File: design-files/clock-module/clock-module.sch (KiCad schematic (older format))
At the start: 32 parts, among them J101 CUI_PJ-097BH-5_5-2_5mm-5A, Q101 2N6491, SW101 SW_Push, SW102 SW_SPDT, SW103 SW_SPDT, U101 NE555P, U102 NE555P, U103 NE555P, U104 74HCT00, U105 74HCT00

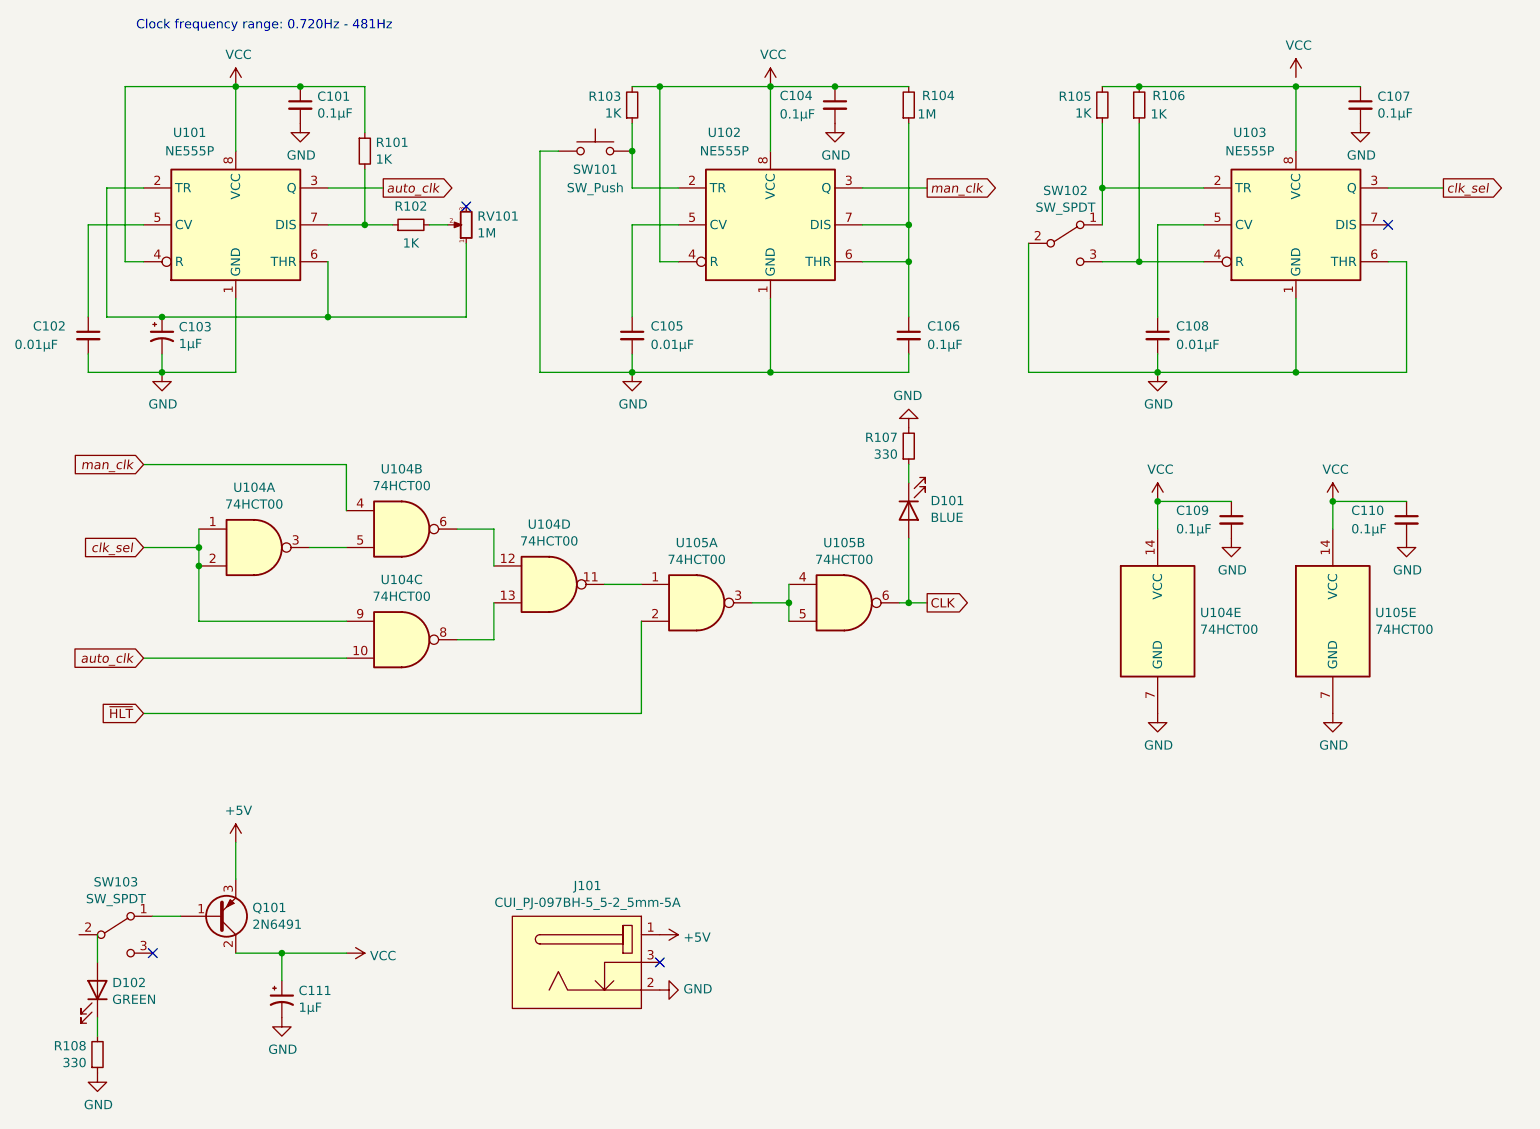
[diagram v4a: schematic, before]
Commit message: clock module: - Don't show the value for each part of a multi-unit device. - Use a green LED for the clock visual.
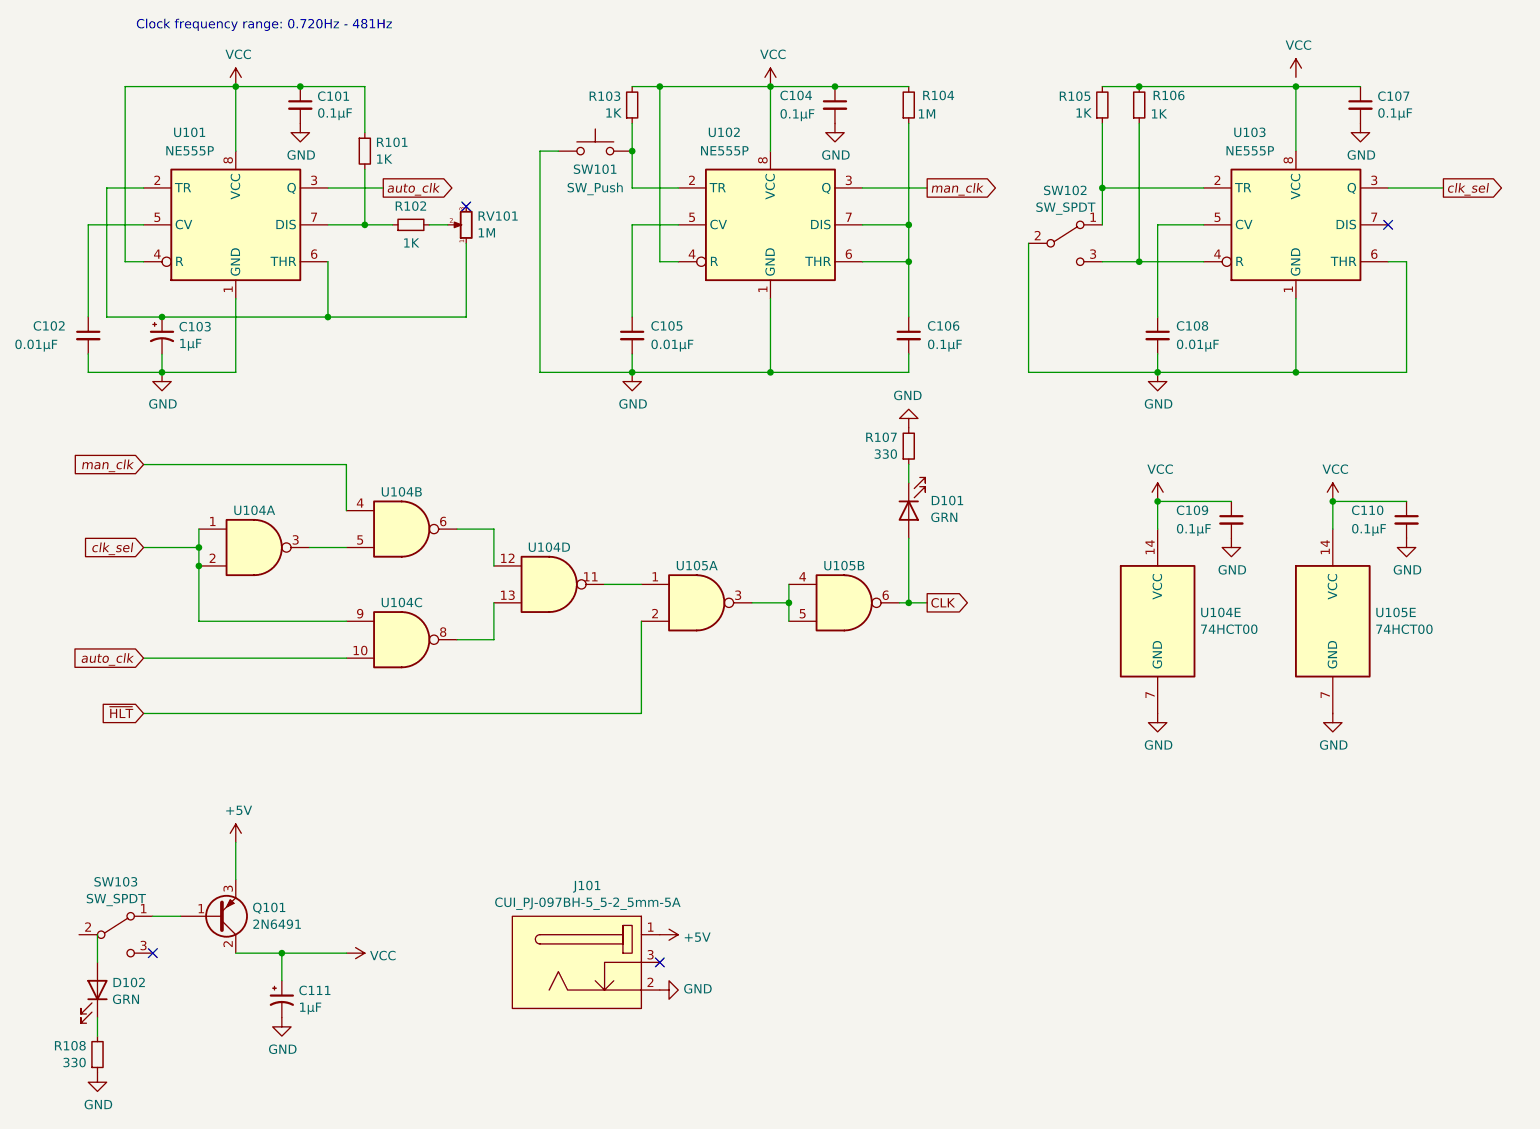
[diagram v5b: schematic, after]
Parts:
- D101: value BLUE -> GRN
- D102: value GREEN -> GRN
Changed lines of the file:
@@
 U 1 1 61BE5527
 P 2250 4050
-F 0 "U104" H 2250 4375 50  0000 C CNN
-F 1 "74HCT00" H 2250 4284 50  0000 C CNN
+F 0 "U104" H 2250 4250 50  0000 C CNN
+F 1 "74HCT00" H 2250 4284 50  0001 C CNN
 F 2 "Package_DIP:DIP-14_W7.62mm_Socket" H 2250 4050 50  0001 C CNN
 F 3 "http://www.ti.com/lit/gpn/sn74hct00" H 2250 4050 50  0001 C CNN
@@
 U 2 1 61BE9444
 P 3050 3950
-F 0 "U104" H 3050 4275 50  0000 C CNN
-F 1 "74HCT00" H 3050 4184 50  0000 C CNN
+F 0 "U104" H 3050 4150 50  0000 C CNN
+F 1 "74HCT00" H 3050 4184 50  0001 C CNN
 F 2 "Package_DIP:DIP-14_W7.62mm_Socket" H 3050 3950 50  0001 C CNN
 F 3 "http://www.ti.com/lit/gpn/sn74hct00" H 3050 3950 50  0001 C CNN
@@
 U 3 1 61BECEBD
 P 3050 4550
-F 0 "U104" H 3050 4875 50  0000 C CNN
-F 1 "74HCT00" H 3050 4784 50  0000 C CNN
+F 0 "U104" H 3050 4750 50  0000 C CNN
+F 1 "74HCT00" H 3050 4784 50  0001 C CNN
 F 2 "Package_DIP:DIP-14_W7.62mm_Socket" H 3050 4550 50  0001 C CNN
 F 3 "http://www.ti.com/lit/gpn/sn74hct00" H 3050 4550 50  0001 C CNN
@@
 U 4 1 61BEEBE7
 P 3850 4250
-F 0 "U104" H 3850 4575 50  0000 C CNN
-F 1 "74HCT00" H 3850 4484 50  0000 C CNN
+F 0 "U104" H 3850 4450 50  0000 C CNN
+F 1 "74HCT00" H 3850 4484 50  0001 C CNN
 F 2 "Package_DIP:DIP-14_W7.62mm_Socket" H 3850 4250 50  0001 C CNN
 F 3 "http://www.ti.com/lit/gpn/sn74hct00" H 3850 4250 50  0001 C CNN
@@
 U 1 1 61C2C1D1
 P 4650 4350
-F 0 "U105" H 4650 4675 50  0000 C CNN
-F 1 "74HCT00" H 4650 4584 50  0000 C CNN
+F 0 "U105" H 4650 4550 50  0000 C CNN
+F 1 "74HCT00" H 4650 4584 50  0001 C CNN
 F 2 "Package_DIP:DIP-14_W7.62mm_Socket" H 4650 4350 50  0001 C CNN
 F 3 "http://www.ti.com/lit/gpn/sn74hct00" H 4650 4350 50  0001 C CNN
@@
 U 2 1 61C30F8B
 P 5450 4350
-F 0 "U105" H 5450 4675 50  0000 C CNN
-F 1 "74HCT00" H 5450 4584 50  0000 C CNN
+F 0 "U105" H 5450 4550 50  0000 C CNN
+F 1 "74HCT00" H 5450 4584 50  0001 C CNN
 F 2 "Package_DIP:DIP-14_W7.62mm_Socket" H 5450 4350 50  0001 C CNN
 F 3 "http://www.ti.com/lit/gpn/sn74hct00" H 5450 4350 50  0001 C CNN
@@
 P 5800 3850
 F 0 "D101" V 5747 3732 50  0000 R CNN
-F 1 "BLUE" V 5838 3732 50  0000 R CNN
+F 1 "GRN" V 5838 3732 50  0000 R CNN
 F 2 "LED_THT:LED_D5.0mm" H 5800 3850 50  0001 C CNN
 F 3 "~" H 5800 3850 50  0001 C CNN
@@
 P 1400 6450
 F 0 "D102" V 1439 6530 50  0000 L CNN
-F 1 "GREEN" V 1348 6530 50  0000 L CNN
+F 1 "GRN" V 1348 6530 50  0000 L CNN
 F 2 "LED_THT:LED_D5.0mm" H 1400 6450 50  0001 C CNN
 F 3 "~" H 1400 6450 50  0001 C CNN

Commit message: clock-module: switch to a Nichicon electrolytic with a smaller footprint.
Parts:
- C103: footprint Capacitor_THT:CP_Radial_D8.0mm_P5.00mm -> Capacitor_THT:CP_Radial_D6.3mm_P2.50mm; Mouser 667-ECA-2VM010B -> 647-UVY2D010MED1TA
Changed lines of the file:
@@
 F 0 "C103" H 1841 2946 50  0000 L CNN
 F 1 "1µF" H 1841 2855 50  0000 L CNN
-F 2 "Capacitor_THT:CP_Radial_D8.0mm_P5.00mm" H 1750 2900 50  0001 C CNN
+F 2 "Capacitor_THT:CP_Radial_D6.3mm_P2.50mm" H 1750 2900 50  0001 C CNN
 F 3 "~" H 1750 2900 50  0001 C CNN
-F 4 "667-ECA-2VM010B" H 1750 2900 50  0001 C CNN "Mouser"
+F 4 "647-UVY2D010MED1TA" H 1750 2900 50  0001 C CNN "Mouser"
 	1    1750 2900
 	1    0    0    -1

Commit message: clock-module: ...and the other 1uF electrolytic, too.
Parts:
- C111: footprint Capacitor_THT:CP_Radial_D8.0mm_P5.00mm -> Capacitor_THT:CP_Radial_D6.3mm_P2.50mm; Mouser 667-ECA-2VM010B -> 647-UVY2D010MED1TA
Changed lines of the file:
@@
 F 0 "C111" H 2491 6546 50  0000 L CNN
 F 1 "1µF" H 2491 6455 50  0000 L CNN
-F 2 "Capacitor_THT:CP_Radial_D8.0mm_P5.00mm" H 2400 6500 50  0001 C CNN
+F 2 "Capacitor_THT:CP_Radial_D6.3mm_P2.50mm" H 2400 6500 50  0001 C CNN
 F 3 "~" H 2400 6500 50  0001 C CNN
-F 4 "667-ECA-2VM010B" H 2400 6500 50  0001 C CNN "Mouser"
+F 4 "647-UVY2D010MED1TA" H 2400 6500 50  0001 C CNN "Mouser"
 	1    2400 6500
 	1    0    0    -1

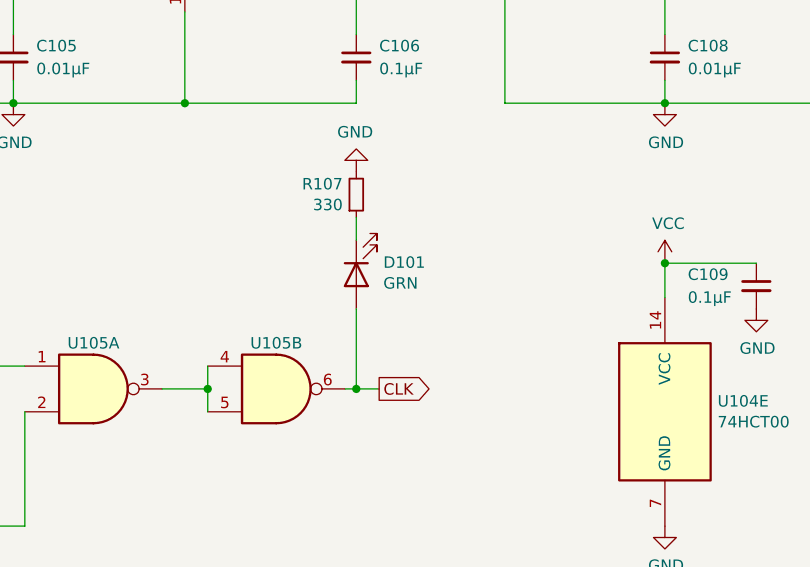
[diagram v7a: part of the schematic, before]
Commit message: Use a yellow / amber LED for the clock pulse.
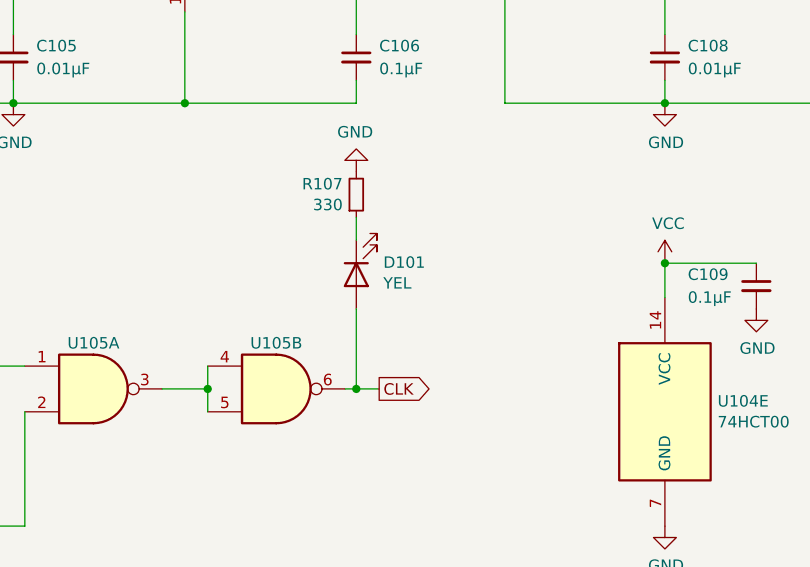
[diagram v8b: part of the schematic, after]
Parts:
- D101: value GRN -> YEL; Mouser 941-C503BBCSCW0X0452 -> 941-C503BACNCX0Y0342
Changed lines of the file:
@@
 P 5800 3850
 F 0 "D101" V 5747 3732 50  0000 R CNN
-F 1 "GRN" V 5838 3732 50  0000 R CNN
+F 1 "YEL" V 5838 3732 50  0000 R CNN
 F 2 "LED_THT:LED_D5.0mm" H 5800 3850 50  0001 C CNN
 F 3 "~" H 5800 3850 50  0001 C CNN
-F 4 "941-C503BBCSCW0X0452" V 5800 3850 50  0001 C CNN "Mouser"
+F 4 "941-C503BACNCX0Y0342" V 5800 3850 50  0001 C CNN "Mouser"
 	1    5800 3850
 	0    -1   1    0
